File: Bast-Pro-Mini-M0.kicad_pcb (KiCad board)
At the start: 2 copper layers, 17.8 x 33 mm, 24 parts, among them J1 USB_B_Micro, J2 Conn_02x02_Odd_Even, P1 Digital, P2 ADC, P4 Analog, U1 AP2112K-3.3TRG1, U2 ATSAMD21E18A-AF

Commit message: label v0.1 add
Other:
- board text added: "v0.1"
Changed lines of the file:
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@@
   (general
     (thickness 1.6)
-    (drawings 46)
+    (drawings 47)
     (tracks 486)
     (zones 0)
@@
   )
   (layers
-    (0 F.Cu signal)
-    (31 B.Cu signal)
+    (0 F.Cu signal hide)
+    (31 B.Cu signal hide)
     (32 B.Adhes user)
     (33 F.Adhes user)
@@
     )
   )
+  (gr_text v0.1 (at 146.7 102.45) (layer B.SilkS)
+    (effects (font (size 1 1) (thickness 0.25)) (justify mirror))
+  )
   (gr_text . (at 150.5 101.5) (layer F.SilkS)

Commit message: bast revision
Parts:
- moved C5 1.23 mm to (149.7, 112.1), turned to 90 degrees
- moved C4 0.22 mm to (150.2, 108.5)
- moved PWR 0.09 mm to (148.4, 89.9)
- renumbered P4 to P3
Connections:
- C3 pad 1: Net-(C3-Pad1) -> +3V3
- P3 pad 1: /RAW -> VCC
- P3 pad 3: /Reset -> /RESET
- P3 pad 4: VCC -> +3V3
- U2 pad 9: Net-(C3-Pad1) -> +3V3
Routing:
- net /RESET: track 37.9 -> 69.0 mm, vias 3 -> 6
- net +3V3: track 66.2 -> 89.3 mm, vias 3 -> 5
- net GND: track 90.1 -> 103.9 mm, vias 8 -> 9
- net VCC: track 12.0 -> 22.9 mm
- net /D+: track 31.4 -> 27.9 mm
- net /0(Rx): track 30.8 -> 33.6 mm
- net Net-(C3-Pad1): track 2.34 -> 0.00 mm
- net /1(Tx): track 31.7 -> 32.9 mm

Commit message: Fix tracks and update revision
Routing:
- net /D+: track 27.9 -> 28.5 mm
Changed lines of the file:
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@@
-(kicad_pcb (version 20171130) (host pcbnew "(5.0.0)")
+(kicad_pcb (version 20171130) (host pcbnew "(5.0.0-3-g5ebb6b6)")
   (general
     (thickness 1.6)
     (drawings 47)
-    (tracks 614)
+    (tracks 612)
     (zones 0)
     (modules 24)
@@
   (title_block
     (title "Bast Pro Mini M0 ")
-    (date 2018-10-31)
-    (rev 0.1)
+    (date 2018-11-09)
+    (rev 0.2)
     (company "Electronic Cats")
     (comment 1 "Eduardo Contreras")
@@
   (gr_line (start 137.16 81.28) (end 154.94 81.28) (angle 90) (layer Edge.Cuts) (width 0.1))
   (gr_line (start 137.16 114.3) (end 137.16 81.28) (angle 90) (layer Edge.Cuts) (width 0.1))
-  (via (at 145.28 92.73) (size 0.8) (drill 0.5) (layers F.Cu B.Cu) (net 21))
   (via (at 151.71 100.4) (size 0.8) (drill 0.5) (layers F.Cu B.Cu) (net 1))
   (segment (start 150.985103 101.474695) (end 151.85 100.609798) (width 0.3) (layer F.Cu) (net 1))
@@
   (segment (start 150.88566 106.18) (end 150.95566 106.25) (width 0.3) (layer B.Cu) (net 20))
   (segment (start 150.88566 106.18) (end 147.45 102.74434) (width 0.3) (layer B.Cu) (net 20))
+  (via (at 145.28 92.73) (size 0.8) (drill 0.5) (layers F.Cu B.Cu) (net 21))
   (segment (start 143.5 88.9) (end 143.6 88.8) (width 0.3) (layer B.Cu) (net 21))
   (segment (start 141.5 88.9) (end 143.5 88.9) (width 0.3) (layer B.Cu) (net 21))
@@
   (segment (start 140.033431 113.175) (end 140.033431 110.785183) (width 0.3) (layer F.Cu) (net 21))
   (segment (start 148.077065 113.597945) (end 140.675 113.597945) (width 0.3) (layer F.Cu) (net 21))
-  (segment (start 142.95 90.8) (end 142.95 91.73) (width 0.3) (layer F.Cu) (net 21))
-  (segment (start 142.74 91.87) (end 142.81 91.87) (width 0.3) (layer F.Cu) (net 21))
-  (segment (start 142.81 91.87) (end 142.95 91.73) (width 0.3) (layer F.Cu) (net 21))
   (segment (start 140.325 110.65) (end 140.325 110.84717) (width 0.3) (layer B.Cu) (net 21))
   (segment (start 140.675 110.3) (end 140.325 110.65) (width 0.3) (layer B.Cu) (net 21))
@@
   (segment (start 141.274635 106.541363) (end 140.675 107.140998) (width 0.3) (layer B.Cu) (net 21))
   (segment (start 141.274635 93.25) (end 141.274635 106.541363) (width 0.3) (layer B.Cu) (net 21))
-  (segment (start 142.32 91.88) (end 142.885685 91.88) (width 0.3) (layer F.Cu) (net 21))
-  (segment (start 142.885685 91.88) (end 142.95 91.815685) (width 0.3) (layer F.Cu) (net 21))
-  (segment (start 142.95 91.815685) (end 142.95 91.73) (width 0.3) (layer F.Cu) (net 21))
   (segment (start 141.5 88.9) (end 140.925 88.9) (width 0.3) (layer B.Cu) (net 21))
   (segment (start 140.925 88.9) (end 140.475 89.35) (width 0.3) (layer B.Cu) (net 21))
@@
   (segment (start 149.49 92.24) (end 151.884 92.24) (width 0.3) (layer F.Cu) (net 21))
   (segment (start 151.884 92.24) (end 152.354 92.71) (width 0.3) (layer F.Cu) (net 21))
+  (segment (start 143.18 91.02) (end 142.32 91.88) (width 0.3) (layer F.Cu) (net 21))
+  (segment (start 143.18 90.7) (end 143.18 91.02) (width 0.3) (layer F.Cu) (net 21))
   (segment (start 149.783021 105.717335) (end 149.288047 105.222361) (width 0.3) (layer F.Cu) (net 22))
   (segment (start 149.783021 106.633021) (end 149.783021 105.717335) (width 0.3) (layer F.Cu) (net 22))
@@
   (segment (start 141.09 85.9) (end 140.88 85.69) (width 0.3) (layer B.Cu) (net 31))
   (segment (start 141.09 86.11) (end 141.09 85.9) (width 0.3) (layer B.Cu) (net 31))
-  (segment (start 140.88 84.45001) (end 140.88 85.69) (width 0.3) (layer F.Cu) (net 31))
-  (segment (start 141.17 84.16001) (end 140.88 84.45001) (width 0.3) (layer F.Cu) (net 31))
-  (segment (start 153.51 82.4) (end 153.110001 82.000001) (width 0.3) (layer F.Cu) (net 31))
-  (segment (start 153.110001 82.000001) (end 151.479999 82.000001) (width 0.3) (layer F.Cu) (net 31))
-  (segment (start 151.479999 82.000001) (end 150.90001 82.57999) (width 0.3) (layer F.Cu) (net 31))
-  (segment (start 150.90001 82.57999) (end 150.90001 83.84999) (width 0.3) (layer F.Cu) (net 31))
-  (segment (start 150.90001 83.84999) (end 150.58999 84.16001) (width 0.3) (layer F.Cu) (net 31))
-  (segment (start 150.58999 84.16001) (end 141.17 84.16001) (width 0.3) (layer F.Cu) (net 31))
+  (segment (start 153.110001 82.000001) (end 153.51 82.4) (width 0.3) (layer F.Cu) (net 31))
+  (segment (start 150.90001 83.84999) (end 150.90001 82.57999) (width 0.3) (layer F.Cu) (net 31))
+  (segment (start 150.58999 84.16001) (end 150.90001 83.84999) (width 0.3) (layer F.Cu) (net 31))
+  (segment (start 140.88 84.68001) (end 141.4 84.16001) (width 0.3) (layer F.Cu) (net 31))
+  (segment (start 151.479999 82.000001) (end 153.110001 82.000001) (width 0.3) (layer F.Cu) (net 31))
+  (segment (start 150.90001 82.57999) (end 151.479999 82.000001) (width 0.3) (layer F.Cu) (net 31))
+  (segment (start 141.4 84.16001) (end 150.58999 84.16001) (width 0.3) (layer F.Cu) (net 31))
+  (segment (start 140.88 85.69) (end 140.88 84.68001) (width 0.3) (layer F.Cu) (net 31))
   (segment (start 144.40901 106.919417) (end 143.628427 107.7) (width 0.3) (layer F.Cu) (net 32))
   (segment (start 143.628427 107.7) (end 142.6 107.7) (width 0.3) (layer F.Cu) (net 32))
@@
   (segment (start 146.14999 90.923008) (end 146.14999 87.494992) (width 0.3) (layer F.Cu) (net 33))
   (segment (start 146.14999 87.494992) (end 146.074999 87.420001) (width 0.3) (layer F.Cu) (net 33))
+  (segment (start 144.255832 91.92) (end 144.320414 91.984582) (width 0.3) (layer F.Cu) (net 33))
+  (segment (start 143.67 91.92) (end 144.255832 91.92) (width 0.3) (layer F.Cu) (net 33))
   (segment (start 141.65 91) (end 141.2 90.55) (width 0.3) (layer F.Cu) (net 34))
   (segment (start 142.146268 100.343324) (end 141.65 99.847056) (width 0.3) (layer F.Cu) (net 34))

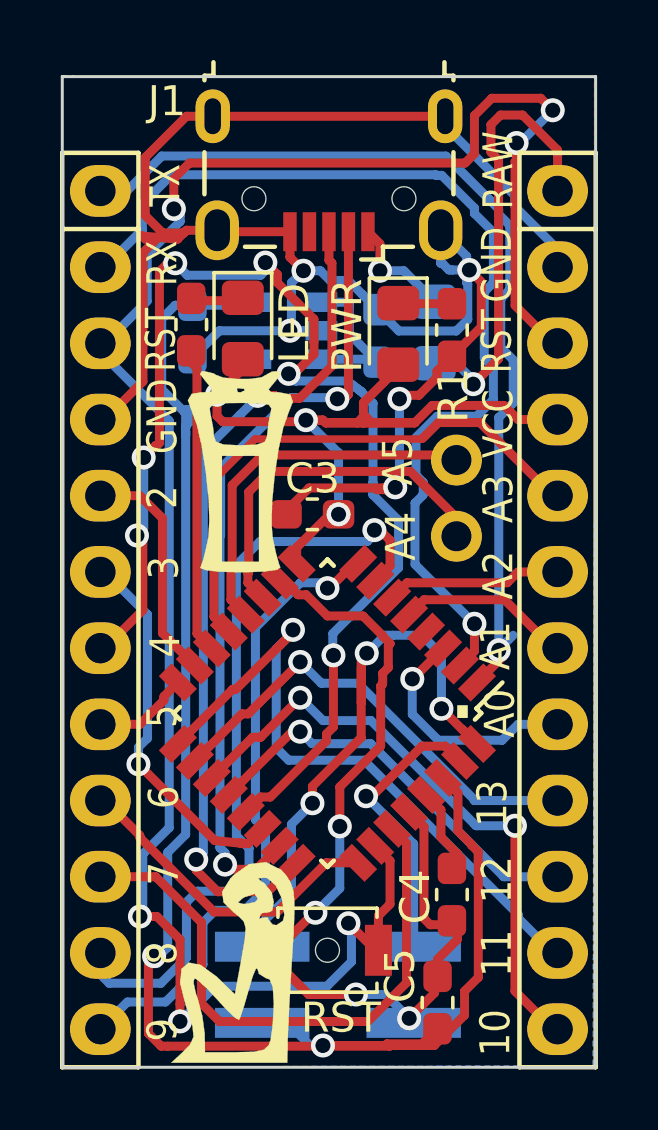
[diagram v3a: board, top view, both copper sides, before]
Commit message: Fix vias, add version on board
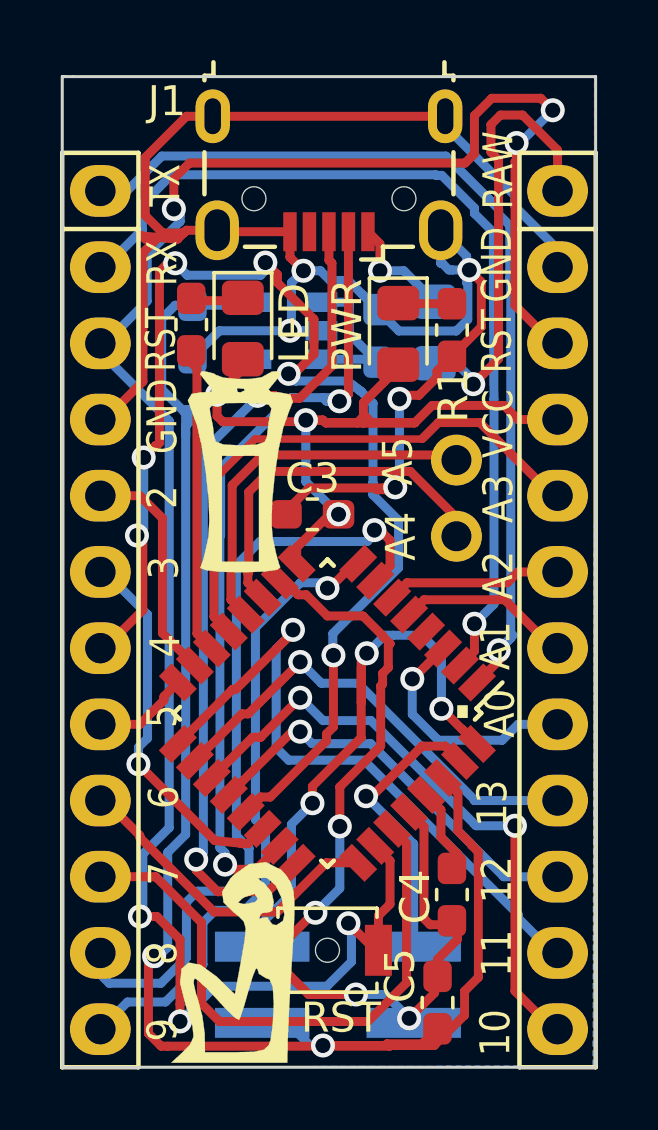
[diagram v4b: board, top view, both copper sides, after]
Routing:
- net /0(Rx): track 33.6 -> 30.7 mm
- net /D-: track 26.3 -> 26.9 mm
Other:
- board text added: "v0.2"
- board text removed: "v0.1"
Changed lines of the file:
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@@
     (thickness 1.6)
     (drawings 47)
-    (tracks 612)
+    (tracks 601)
     (zones 0)
     (modules 24)
@@
   )
   (layers
-    (0 F.Cu signal)
-    (31 B.Cu signal)
+    (0 F.Cu signal hide)
+    (31 B.Cu signal hide)
     (32 B.Adhes user)
     (33 F.Adhes user)
@@
     )
   )
-  (gr_text v0.1 (at 146.7 102.45) (layer B.SilkS)
+  (gr_text v0.2 (at 146.7 102.45) (layer B.SilkS)
     (effects (font (size 1 1) (thickness 0.25)) (justify mirror))
   )
@@
   (segment (start 151.703982 85.866152) (end 151.703982 85.685145) (width 0.3) (layer B.Cu) (net 1))
   (segment (start 152.08001 86.24218) (end 151.703982 85.866152) (width 0.3) (layer B.Cu) (net 1))
-  (segment (start 151.71 100.4) (end 151.71 92.641832) (width 0.3) (layer B.Cu) (net 1))
-  (segment (start 151.71 92.641832) (end 152.19 92.161832) (width 0.3) (layer B.Cu) (net 1))
-  (segment (start 152.19 92.161832) (end 152.19 90.72) (width 0.3) (layer B.Cu) (net 1))
-  (segment (start 152.19 90.72) (end 151.778366 90.308366) (width 0.3) (layer B.Cu) (net 1))
-  (segment (start 152.08001 88.377821) (end 152.08001 86.24218) (width 0.3) (layer B.Cu) (net 1))
-  (segment (start 151.778366 90.308366) (end 151.778366 88.679465) (width 0.3) (layer B.Cu) (net 1))
-  (segment (start 151.778366 88.679465) (end 152.08001 88.377821) (width 0.3) (layer B.Cu) (net 1))
   (segment (start 140.477602 83.9264) (end 149.945237 83.9264) (width 0.3) (layer B.Cu) (net 1))
   (segment (start 149.945237 83.9264) (end 151.3 85.281163) (width 0.3) (layer B.Cu) (net 1))
   (segment (start 139.314002 85.09) (end 140.477602 83.9264) (width 0.3) (layer B.Cu) (net 1))
   (segment (start 138.43 85.09) (end 139.314002 85.09) (width 0.3) (layer B.Cu) (net 1))
+  (segment (start 152.109999 100.000001) (end 151.71 100.4) (width 0.3) (layer B.Cu) (net 1))
+  (segment (start 152.109999 88.029989) (end 152.109999 100.000001) (width 0.3) (layer B.Cu) (net 1))
+  (segment (start 152.08001 88) (end 152.109999 88.029989) (width 0.3) (layer B.Cu) (net 1))
+  (segment (start 152.08001 88) (end 152.08001 86.24218) (width 0.3) (layer B.Cu) (net 1))
   (via (at 150.9 99.516979) (size 0.8) (drill 0.5) (layers F.Cu B.Cu) (net 2))
   (segment (start 150.419417 100.90901) (end 150.9 100.428427) (width 0.3) (layer F.Cu) (net 2))
   (segment (start 150.9 100.428427) (end 150.9 99.516979) (width 0.3) (layer F.Cu) (net 2))
-  (segment (start 149.19 94.800002) (end 149.19 95.224002) (width 0.3) (layer B.Cu) (net 2))
-  (segment (start 148.95001 94.560012) (end 149.19 94.800002) (width 0.3) (layer B.Cu) (net 2))
-  (segment (start 148.95001 93.30999) (end 148.95001 94.560012) (width 0.3) (layer B.Cu) (net 2))
-  (segment (start 148.920011 95.493991) (end 148.920011 97.53699) (width 0.3) (layer B.Cu) (net 2))
-  (segment (start 149.66 92.6) (end 148.95001 93.30999) (width 0.3) (layer B.Cu) (net 2))
-  (segment (start 150.974002 92.6) (end 149.66 92.6) (width 0.3) (layer B.Cu) (net 2))
-  (segment (start 149.19 95.224002) (end 148.920011 95.493991) (width 0.3) (layer B.Cu) (net 2))
-  (segment (start 151.53 92.044002) (end 150.974002 92.6) (width 0.3) (layer B.Cu) (net 2))
   (segment (start 149.609999 84.549999) (end 149.63 84.57) (width 0.3) (layer B.Cu) (net 2))
   (segment (start 140.810001 84.549999) (end 149.609999 84.549999) (width 0.3) (layer B.Cu) (net 2))
   (segment (start 139.83 85.53) (end 140.810001 84.549999) (width 0.3) (layer B.Cu) (net 2))
-  (segment (start 151.228356 90.668356) (end 151.46 90.9) (width 0.3) (layer B.Cu) (net 2))
   (segment (start 139.83 86.3824) (end 139.83 85.53) (width 0.3) (layer B.Cu) (net 2))
-  (segment (start 151.46 90.9) (end 151.53 90.9) (width 0.3) (layer B.Cu) (net 2))
-  (segment (start 151.228356 88.451644) (end 151.228356 90.668356) (width 0.3) (layer B.Cu) (net 2))
   (segment (start 138.5824 87.63) (end 139.83 86.3824) (width 0.3) (layer B.Cu) (net 2))
   (segment (start 138.43 87.63) (end 138.5824 87.63) (width 0.3) (layer B.Cu) (net 2))
@@
   (segment (start 150.90001 85.659006) (end 150.90001 85.84001) (width 0.3) (layer B.Cu) (net 2))
   (segment (start 151.53 86.47) (end 151.53 88.15) (width 0.3) (layer B.Cu) (net 2))
-  (segment (start 148.920011 97.53699) (end 150.9 99.516979) (width 0.3) (layer B.Cu) (net 2))
-  (segment (start 151.53 88.15) (end 151.228356 88.451644) (width 0.3) (layer B.Cu) (net 2))
   (segment (start 150.90001 85.84001) (end 151.53 86.47) (width 0.3) (layer B.Cu) (net 2))
-  (segment (start 151.53 90.9) (end 151.53 92.044002) (width 0.3) (layer B.Cu) (net 2))
+  (segment (start 151.550001 98.866978) (end 151.550001 92.024001) (width 0.3) (layer B.Cu) (net 2))
+  (segment (start 150.9 99.516979) (end 151.550001 98.866978) (width 0.3) (layer B.Cu) (net 2))
+  (segment (start 151.53 88.15) (end 151.550001 92.024001) (width 0.3) (layer B.Cu) (net 2))
   (segment (start 142.175 82.6) (end 149.925 82.6) (width 0.3) (layer F.Cu) (net 3))
   (via (at 145.2 87.75) (size 0.8) (drill 0.5) (layers F.Cu B.Cu) (net 3))
@@
   (segment (start 140.40001 93.48999) (end 140.40001 87.774305) (width 0.3) (layer F.Cu) (net 6))
   (segment (start 140.634315 87.54) (end 140.84 87.54) (width 0.3) (layer F.Cu) (net 6))
-  (segment (start 146.18 100.55) (end 146.2 100.57) (width 0.3) (layer B.Cu) (net 6))
-  (segment (start 146.18 99.845179) (end 146.18 100.55) (width 0.3) (layer B.Cu) (net 6))
-  (segment (start 147.130001 91.780001) (end 147.52 92.17) (width 0.3) (layer B.Cu) (net 6))
-  (segment (start 148.370001 97.655178) (end 146.18 99.845179) (width 0.3) (layer B.Cu) (net 6))
-  (segment (start 147.52 92.17) (end 147.52 94.82) (width 0.3) (layer B.Cu) (net 6))
-  (segment (start 148.370001 96.070001) (end 148.370001 97.655178) (width 0.3) (layer B.Cu) (net 6))
-  (segment (start 147.52 94.82) (end 147.51 94.83) (width 0.3) (layer B.Cu) (net 6))
-  (segment (start 147.51 94.83) (end 147.51 95.21) (width 0.3) (layer B.Cu) (net 6))
-  (segment (start 147.51 95.21) (end 148.370001 96.070001) (width 0.3) (layer B.Cu) (net 6))
   (via (at 140.926771 87.50001) (size 0.8) (drill 0.5) (layers F.Cu B.Cu) (net 6))
   (segment (start 143.97 87.7) (end 143.769991 87.900009) (width 0.3) (layer B.Cu) (net 6))
   (segment (start 141.32677 87.900009) (end 140.926771 87.50001) (width 0.3) (layer B.Cu) (net 6))
   (segment (start 143.769991 87.900009) (end 141.32677 87.900009) (width 0.3) (layer B.Cu) (net 6))
+  (segment (start 147.52 92.17) (end 147.130001 91.780001) (width 0.3) (layer B.Cu) (net 6))
+  (segment (start 147.52 94.82) (end 147.52 92.17) (width 0.3) (layer B.Cu) (net 6))
+  (segment (start 147.51 94.83) (end 147.52 94.82) (width 0.3) (layer B.Cu) (net 6))
+  (segment (start 148.370001 97.655178) (end 148.370001 96.070001) (width 0.3) (layer B.Cu) (net 6))
+  (segment (start 146.18 99.845179) (end 148.370001 97.655178) (width 0.3) (layer B.Cu) (net 6))
+  (segment (start 148.370001 96.070001) (end 147.51 95.21) (width 0.3) (layer B.Cu) (net 6))
+  (segment (start 146.18 100.55) (end 146.18 99.845179) (width 0.3) (layer B.Cu) (net 6))
+  (segment (start 147.51 95.21) (end 147.51 94.83) (width 0.3) (layer B.Cu) (net 6))
+  (segment (start 146.2 100.57) (end 146.18 100.55) (width 0.3) (layer B.Cu) (net 6))
   (segment (start 138.43 102.87) (end 138.5824 102.87) (width 0.3) (layer F.Cu) (net 7))
   (segment (start 138.85 102.45) (end 138.43 102.87) (width 0.3) (layer B.Cu) (net 7))
@@
   (segment (start 144.974695 97.514897) (end 144.974695 96.975305) (width 0.3) (layer F.Cu) (net 21))
   (via (at 146.37 95.87) (size 0.8) (drill 0.5) (layers F.Cu B.Cu) (net 21))
-  (segment (start 146.37 93.82) (end 146.37 95.87) (width 0.3) (layer B.Cu) (net 21))
-  (segment (start 145.28 92.73) (end 146.37 93.82) (width 0.3) (layer B.Cu) (net 21))
   (segment (start 142.32 92.595) (end 142.32 91.88) (width 0.3) (layer F.Cu) (net 21))
   (segment (start 142.505 92.78) (end 142.32 92.595) (width 0.3) (layer F.Cu) (net 21))
@@
   (segment (start 143.18 91.02) (end 142.32 91.88) (width 0.3) (layer F.Cu) (net 21))
   (segment (start 143.18 90.7) (end 143.18 91.02) (width 0.3) (layer F.Cu) (net 21))
+  (segment (start 145.28 94.78) (end 145.28 92.73) (width 0.3) (layer B.Cu) (net 21))
+  (segment (start 146.37 95.87) (end 145.28 94.78) (width 0.3) (layer B.Cu) (net 21))
   (segment (start 149.783021 105.717335) (end 149.288047 105.222361) (width 0.3) (layer F.Cu) (net 22))
   (segment (start 149.783021 106.633021) (end 149.783021 105.717335) (width 0.3) (layer F.Cu) (net 22))
@@
   (segment (start 143.628427 107.7) (end 142.6 107.7) (width 0.3) (layer F.Cu) (net 32))
   (via (at 142.586192 107.545193) (size 0.8) (drill 0.5) (layers F.Cu B.Cu) (net 32))
-  (via (at 146.33 92.02) (size 0.8) (drill 0.5) (layers F.Cu B.Cu) (net 32))
   (segment (start 142.586192 107.15219) (end 142.415152 106.98115) (width 0.3) (layer B.Cu) (net 32))
   (segment (start 142.586192 107.545193) (end 142.586192 107.15219) (width 0.3) (layer B.Cu) (net 32))
@@
   (segment (start 146.7 91.872167) (end 146.5 92.072167) (width 0.3) (layer F.Cu) (net 32))
   (segment (start 146.5 92.072167) (end 146.5 92.21) (width 0.3) (layer F.Cu) (net 32))
-  (segment (start 146.7 86.45) (end 146.7 91.872167) (width 0.3) (layer F.Cu) (net 32))
+  (segment (start 146.7 91.1) (end 146.7 91.872167) (width 0.3) (layer F.Cu) (net 32))
+  (segment (start 146.7 86.45) (end 146.7 91.1) (width 0.3) (layer F.Cu) (net 32))
+  (segment (start 145.97 92.1) (end 145.85 91.98) (width 0.3) (layer B.Cu) (net 32))
+  (segment (start 146.4 92.1) (end 145.97 92.1) (width 0.3) (layer B.Cu) (net 32))
+  (via (at 146.4 92.1) (size 0.8) (drill 0.5) (layers F.Cu B.Cu) (net 32))
   (segment (start 144.974695 107.485103) (end 144.011081 108.448717) (width 0.3) (layer F.Cu) (net 33))
   (segment (start 141.625 107.734002) (end 141.625 107.398716) (width 0.3) (layer F.Cu) (net 33))

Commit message: Update tracks
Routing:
- net /11(**/MOSI): track 22.2 -> 24.7 mm
- net /A0: track 8.04 -> 8.75 mm
- net /D+: track 28.5 -> 29.2 mm
- net /4: track 42.9 -> 43.4 mm
